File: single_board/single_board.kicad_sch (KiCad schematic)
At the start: 124 parts, among them J1 GPIO, J11 SPI Debug, J17 BOOTSEL, J2 USB_C_Receptacle_USB2.0_16P, J3 SWD, J30 JST_GH_H, J31 JST_GH_H, J33 JST_GH_H, J34 PB_Vertical, J35 JST_GH_H, J36 JST_GH_H, J37 JST_GH_H, J38 PB_Vertical, J39 PB_Vertical, J40 PB_Vertical, J41 PB_Vertical, J42 PB_Vertical, J43 PB_Vertical, J44 PB_Vertical, J45 PB_Vertical, J46 PB_Vertical, J47 PB_Vertical, J48 PB_Vertical, J49 PB_Vertical, J5 JST-GH, J50 PB_Vertical, J53 PB_Vertical, J56 Power, Q1 AO3400A, Q3 AO3401A, SW1 Button, U1 AP2112K-3.3, U3 USBLC6-2SC6, U4 LSM6DSV, U5 STM32G474VBTx, Y2 ABM8-16MHz

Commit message: UART Connector
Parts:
- added J54: (no value), rover:2.54 SMD, symbol Connector_Generic:Conn_01x04
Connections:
- net GND: now also J54.1 (Pin_1), J54.4 (Pin_4)
- net USART3_RX: now also J54.3 (Pin_3)
- net USART3_TX: now also J54.2 (Pin_2)
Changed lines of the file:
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@@
 	)
 	(junction
+		(at 388.62 191.77)
+		(diameter 0)
+		(color 0 0 0 0)
+	)
+	(junction
 		(at 311.15 195.58)
 		(diameter 0)
@@
 	(wire
 		(pts
+			(xy 388.62 191.77) (xy 391.16 191.77)
+		)
+		(stroke
+			(width 0)
+			(type default)
+		)
+	)
+	(wire
+		(pts
 			(xy 153.67 368.3) (xy 156.21 368.3)
 		)
@@
 	(wire
 		(pts
+			(xy 372.11 191.77) (xy 388.62 191.77)
+		)
+		(stroke
+			(width 0)
+			(type default)
+		)
+	)
+	(wire
+		(pts
 			(xy 266.7 91.44) (xy 266.7 92.71)
 		)
@@
 	(wire
 		(pts
-			(xy 384.81 196.85) (xy 391.16 196.85)
-		)
-		(stroke
-			(width 0)
-			(type default)
-		)
-	)
-	(wire
-		(pts
 			(xy 64.77 340.36) (xy 67.31 340.36)
 		)
@@
 	(wire
 		(pts
-			(xy 384.81 194.31) (xy 391.16 194.31)
-		)
-		(stroke
-			(width 0)
-			(type default)
-		)
-	)
-	(wire
-		(pts
 			(xy 388.62 298.45) (xy 392.43 298.45)
 		)
@@
 	(wire
 		(pts
-			(xy 388.62 191.77) (xy 391.16 191.77)
-		)
-		(stroke
-			(width 0)
-			(type default)
-		)
-	)
-	(wire
-		(pts
 			(xy 224.79 287.02) (xy 222.25 287.02)
 		)
@@
 	(wire
 		(pts
+			(xy 372.11 196.85) (xy 391.16 196.85)
+		)
+		(stroke
+			(width 0)
+			(type default)
+		)
+	)
+	(wire
+		(pts
 			(xy 67.31 34.29) (xy 76.2 34.29)
 		)
@@
 	(wire
 		(pts
+			(xy 372.11 194.31) (xy 391.16 194.31)
+		)
+		(stroke
+			(width 0)
+			(type default)
+		)
+	)
+	(wire
+		(pts
 			(xy 274.32 176.53) (xy 278.13 176.53)
 		)
@@
 	(wire
 		(pts
+			(xy 372.11 199.39) (xy 388.62 199.39)
+		)
+		(stroke
+			(width 0)
+			(type default)
+		)
+	)
+	(wire
+		(pts
 			(xy 287.02 190.5) (xy 287.02 193.04)
 		)
@@
 					(unit 1)
 				)
+			)
+		)
+	)
+	(symbol
+		(lib_id "Connector_Generic:Conn_01x04")
+		(at 367.03 194.31 0)
+		(mirror y)
+		(unit 1)
+		(body_style 1)
+		(exclude_from_sim no)
+		(in_bom yes)
+		(on_board yes)
+		(in_pos_files yes)
+		(dnp no)
+		(property "Reference" "J54"
+			(at 364.49 194.3099 0)
+			(show_name no)
+			(do_not_autoplace no)
+			(effects
+				(font
+					(size 1.27 1.27)
+				)
+				(justify left)
+			)
+		)
+		(property "Value" ""
+			(at 364.49 196.8499 0)
+			(show_name no)
+			(do_not_autoplace no)
+			(effects
+				(font
+					(size 1.27 1.27)
+				)
+				(justify left)
+			)
+		)
+		(property "Footprint" "rover:2.54 SMD"
+			(at 367.03 194.31 0)
+			(hide yes)
+			(show_name no)
+			(do_not_autoplace no)
+			(effects
+				(font
+					(size 1.27 1.27)
+				)
+			)
+		)
+		(property "Datasheet" ""
+			(at 367.03 194.31 0)
+			(hide yes)
+			(show_name no)
+			(do_not_autoplace no)
+			(effects
+				(font
+					(size 1.27 1.27)
+				)
+			)
+		)
+		(property "Description" "Generic connector, single row, 01x04, script generated (kicad-library-utils/schlib/autogen/connector/)"
+			(at 367.03 194.31 0)
+			(hide yes)
+			(show_name no)
+			(do_not_autoplace no)
+			(effects
+				(font
+					(size 1.27 1.27)
+				)
+			)
+		)
+		(pin "1"
+		)
+		(pin "3"
+		)
+		(pin "4"
+		)
+		(pin "2"
+		)
+		(instances
+			(project "single_board"
+				(path "/ae10586e-ebf8-402d-a979-c2f011cdeee2"
+					(reference "J54")
+					(unit 1)
+				)

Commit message: GPIO
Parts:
- removed J1: GPIO, Connector_PinHeader_2.54mm:PinHeader_2x04_P2.54mm_Vertical, symbol Connector_Generic:Conn_02x04_Counter_Clockwise
- removed J52: (no value), Connector_PinHeader_2.54mm:PinHeader_1x04_P2.54mm_Vertical, symbol Connector_Generic:Conn_01x04
- added J55, J57: PB_Vertical, Connector_Molex:Molex_PicoBlade_53047-0410_1x04_P1.25mm_Vertical, symbol Connector_Generic:Conn_01x04
- added J6: JST-GH, Connector_JST:JST_GH_SM06B-GHS-TB_1x06-1MP_P1.25mm_Horizontal, symbol Connector_Generic_MountingPin:Conn_01x06_MountingPin
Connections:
- net CAN_LED: now also R1.1; no longer D13.2 (A)
- net GND: now also D13.1 (K), D14.1 (K), J55.1 (Pin_1), J55.4 (Pin_4), J57.1 (Pin_1), J57.4 (Pin_4), J6.1 (Pin_1), J6.6 (Pin_6), J6.MP (MountPin); no longer R1.2, R2.2
- net UART_LED: now also R2.1; no longer D14.2 (A)
- net USART3_RX: now also J55.3 (Pin_3)
- net USART3_TX: now also J55.2 (Pin_2)
- net GPIO_1 renamed I2C4_SCL
- net I2C4_SCL: now also R9.2, J57.3 (Pin_3); no longer R7.2
- net GPIO_2 renamed I2C4_SDA
- net I2C4_SDA: now also R7.2, J57.2 (Pin_2); no longer R9.2
- net GPIO_3: no longer names the net of U5.57 (PD10)
- net GPIO_4: no longer names the net of U5.56 (PD9)
- net GPIO_5 renamed SPI2_NSS
- net SPI2_NSS: now also J6.5 (Pin_5)
- net GPIO_6 renamed SPI2_MOSI
- net SPI2_MOSI: now also J6.4 (Pin_4)
- net GPIO_7 renamed SPI2_MISO
- net SPI2_MISO: now also J6.3 (Pin_3)
- net GPIO_8 renamed SPI2_SCK
- net SPI2_SCK: now also J6.2 (Pin_2)
- net I2C_SCL renamed I2C3_SCL
- net I2C_SDA renamed I2C3_SDA
- new net: D13.2 (A), R1.2
- new net: D14.2 (A), R2.2
- no-connect marks 36 -> 38
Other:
- note added: "Current Sensor"
- note added: "GPIO"
- note removed: "I2C3"
- moved on the sheet: C35, C36, D13, D14, J5, J50, J53, J54, R1, R2, R5, R7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

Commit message: Arm Motor Silkscreen
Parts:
- R7, R9: now fitted
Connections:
- net I2C3_SCL: now also J50.2 (Pin_2), R5.2, U5.67 (PC8); no longer J50.3 (Pin_3), R8.2, U5.69 (PA8)
- net I2C3_SDA: now also J50.3 (Pin_3), R8.2; no longer J50.2 (Pin_2), R5.2
- net I2C4_SCL: now also J57.2 (Pin_2), R7.2; no longer J57.3 (Pin_3), R9.2
- net I2C4_SDA: now also J57.3 (Pin_3), R9.2; no longer J57.2 (Pin_2), R7.2
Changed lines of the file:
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@@
 	)
 	(no_connect
-		(at 302.26 309.88)
-	)
-	(no_connect
 		(at 240.03 44.45)
 	)
@@
 	)
 	(no_connect
+		(at 302.26 223.52)
+	)
+	(no_connect
 		(at 570.23 353.06)
 	)
@@
 	)
 	(label "I2C3_SCL"
-		(at 367.03 260.35 180)
+		(at 367.03 257.81 180)
 		(effects
 			(font
@@
 	)
 	(label "I2C3_SCL"
-		(at 302.26 223.52 0)
+		(at 302.26 309.88 0)
 		(effects
 			(font
@@
 	)
 	(label "I2C4_SDA"
-		(at 372.11 342.9 180)
+		(at 372.11 345.44 180)
 		(effects
 			(font
@@
 	)
 	(label "I2C3_SDA"
-		(at 367.03 257.81 180)
+		(at 367.03 260.35 180)
 		(effects
 			(font
@@
 	)
 	(label "I2C4_SCL"
-		(at 372.11 345.44 180)
+		(at 372.11 342.9 180)
 		(effects
 			(font
@@
 		(on_board yes)
 		(in_pos_files yes)
-		(dnp yes)
+		(dnp no)
 		(property "Reference" "R7"
 			(at 381.508 337.566 0)
@@
 		(on_board yes)
 		(in_pos_files yes)
-		(dnp yes)
+		(dnp no)
 		(property "Reference" "R9"
 			(at 387.858 337.566 0)

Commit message: Routing I2C
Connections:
- net IMU_MOSI: now also J11.3 (Pin_3); no longer J11.4 (Pin_4)
- net IMU_SCK: now also J11.4 (Pin_4); no longer J11.3 (Pin_3)
- net INT1: now also U5.32 (PB0); no longer U5.31 (PC5)
- net INT2: now also U5.31 (PC5); no longer U5.32 (PB0)
- net LED4: now also U5.47 (PB10); no longer U5.46 (PE15)
- net LED5: now also U5.46 (PE15); no longer U5.47 (PB10)
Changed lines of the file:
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@@
 	)
 	(label "LED5"
-		(at 302.26 271.78 0)
-		(effects
-			(font
-				(size 1.27 1.27)
-			)
-			(justify left bottom)
+		(at 256.54 266.7 180)
+		(effects
+			(font
+				(size 1.27 1.27)
+			)
+			(justify right bottom)
 		)
 	)
@@
 	)
 	(label "LED4"
-		(at 256.54 266.7 180)
-		(effects
-			(font
-				(size 1.27 1.27)
-			)
-			(justify right bottom)
+		(at 302.26 271.78 0)
+		(effects
+			(font
+				(size 1.27 1.27)
+			)
+			(justify left bottom)
 		)
 	)
 	(label "IMU_MOSI"
-		(at 506.73 274.32 0)
+		(at 506.73 276.86 0)
 		(effects
 			(font
@@
 	)
 	(label "INT2"
-		(at 302.26 246.38 0)
+		(at 302.26 302.26 0)
 		(effects
 			(font
@@
 	)
 	(label "IMU_SCK"
-		(at 506.73 276.86 0)
+		(at 506.73 274.32 0)
 		(effects
 			(font
@@
 	)
 	(label "INT1"
-		(at 302.26 302.26 0)
-		(effects
-			(font
+		(at 302.26 246.38 0)
+		(effects
+			(font

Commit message: Reanotate
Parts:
- renumbered C30 to C1, C38 to C10, C40 to C11, C39 to C12, C11 to C13, C41 to C14, C14 to C15, C15 to C16, C16 to C17, C17 to C18, C18 to C19, C32 to C2, C19 to C20, C20 to C21, C21 to C22, C22 to C23, C23 to C24, C24 to C25, C25 to C26, C26 to C27, C27 to C28, C12 to C29, C33 to C3, C13 to C30, C28 to C31, C34 to C32, C36 to C33, C35 to C34, C10 to C4, C31 to C5, C3 to C6, C6 to C7, C29 to C8, C37 to C9, D2 to D1, D15 to D10, D13 to D11, D14 to D12, D4 to D2, D1 to D3, D5 to D4, D8 to D5, D9 to D6, D10 to D7, D11 to D8, D12 to D9, J34 to J1, J46 to J10, J41 to J11, J54 to J12, J55 to J13, J47 to J14, J42 to J15, J53 to J16, J5 to J17, J43 to J18, J48 to J19, J3 to J2, J50 to J20, J44 to J21, J49 to J22, J11 to J23, J17 to J24, J6 to J25, J31 to J26, J30 to J27, J36 to J28, J57 to J29, J56 to J3, J37 to J30, J33 to J31, J2 to J4, J35 to J5, J39 to J6, J38 to J7, J40 to J8, J45 to J9, Q3 to Q1, Q1 to Q2, R14 to R1, R11 to R10, R12 to R11, R13 to R12, R16 to R13, R17 to R14, R20 to R15, R1 to R16, R2 to R17, R10 to R18, R15 to R2, R5 to R20, R8 to R21, R26 to R22, R27 to R23, R38 to R24, R21 to R25, R29 to R26, R7 to R27, R9 to R28, R39 to R29, R37 to R3, R22 to R30, R40 to R31, R24 to R32, R41 to R33, R30 to R34, R6 to R5, R23 to R6, R33 to R7, R34 to R8, R31 to R9, U3 to U2, U6 to U3, Y2 to Y1

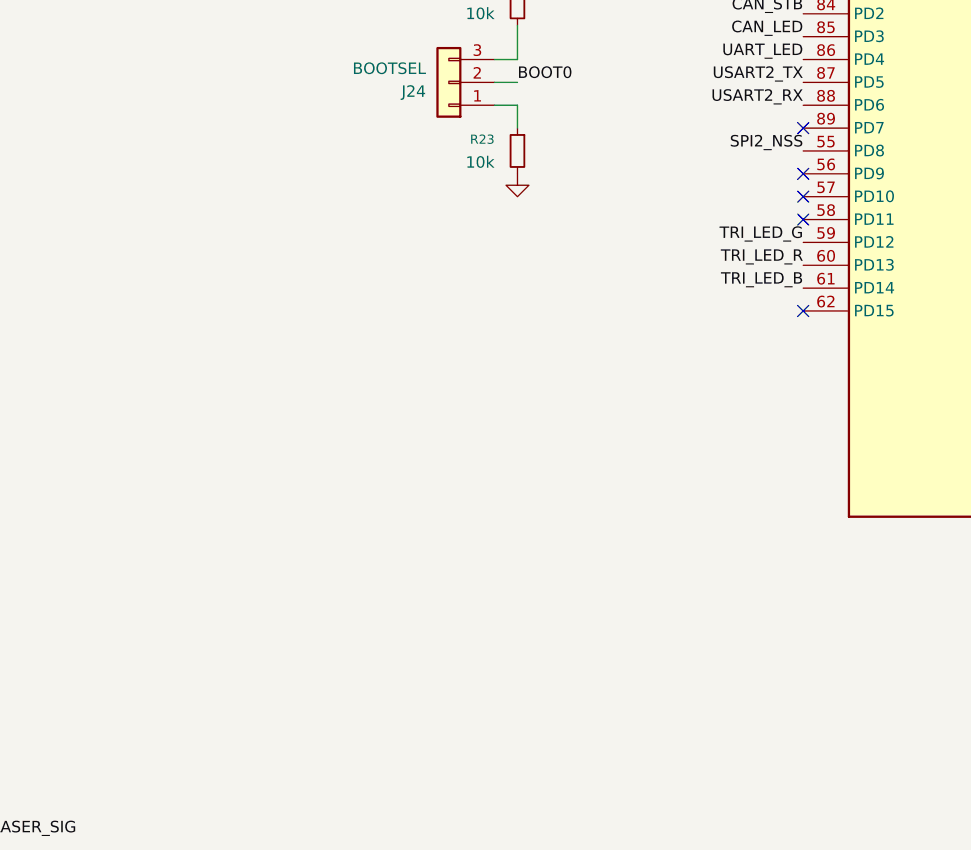
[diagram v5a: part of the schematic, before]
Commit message: 2 User buttons
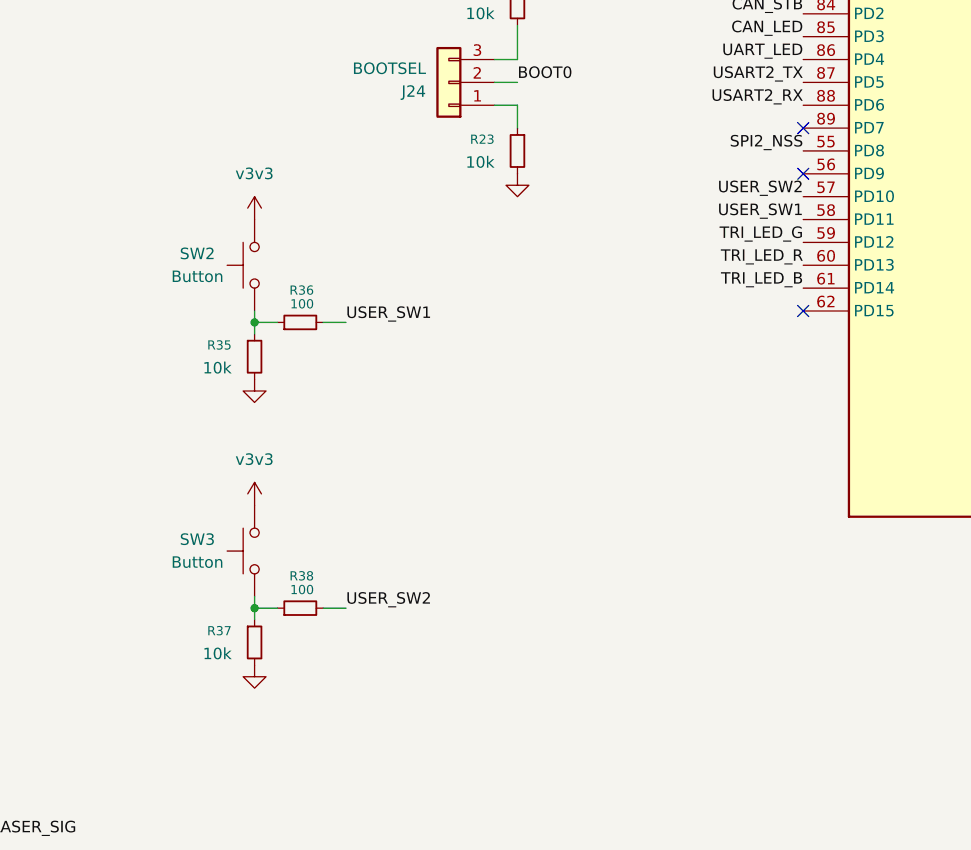
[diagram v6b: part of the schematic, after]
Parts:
- added R35, R37: 10k, Resistor_SMD:R_0402_1005Metric, symbol Device:R_Small
- added R36, R38: 100, Resistor_SMD:R_0402_1005Metric, symbol Device:R_Small
- added SW2, SW3: Button, Button_Switch_SMD:SW_SPST_PTS810, symbol Switch:SW_Push
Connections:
- net GND: now also R35.2, R37.2
- net v3v3: now also SW2.2, SW3.2
- net USER_SW2: now reaches U5.57 (PD10)
- net USER_SW2: now also R38.2
- net USER_SW1: now reaches U5.58 (PD11)
- net USER_SW1: now also R36.2
- new net: R37.1, R38.1, SW3.1
- new net: R35.1, R36.1, SW2.1
- no-connect marks 38 -> 36

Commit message: Production File Setup
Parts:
- C1, C2, C3, C4, C5, C8: LCSC Part # (none) -> C602037
- C10, C11, C13, C20, C21, C22, C23, C24, C28, C29, C30, C31: LCSC Part # (none) -> C100072
- C12, C15, C16, C17, C18, C19, C26, C27, C6, C7, C9: LCSC Part # (none) -> C52923
- C14, C25, C32: LCSC Part # (none) -> C15195
- C33, C34: LCSC Part # (none) -> C76946
- D1, D10, D11, D12, D2, D5, D6, D7, D8, D9: LCSC Part # (none) -> C5160697
- D3: LCSC Part # (none) -> C236208
- D4: LCSC Part # (none) -> C601684
- J1, J10, J11, J13, J14, J15, J16, J18, J19, J20, J21, J22, J29, J6, J7, J8, J9: LCSC Part # (none) -> C504989
- J12: value (none) -> 2.54; now left out of the parts list
- J17, J25: LCSC Part # (none) -> C133065
- J2, J24, TP1, TP2: now left out of the parts list
- J26, J27, J28, J30, J31, J5: value JST_GH_H -> JST_GH; LCSC Part # (none) -> C189893; now left out of the parts list
- J4: LCSC Part # (none) -> C165948
- Q1: LCSC Part # (none) -> C347476
- Q2: LCSC Part # (none) -> C347475
- R1, R10, R11, R12, R13, R14, R15, R16, R17, R18, R19, R2, R22, R23, R25, R30, R32, R34, R35, R37, R6, R9: LCSC Part # (none) -> C71617
- R20, R21, R27, R28, R4, R5: LCSC Part # (none) -> C105872
- R24, R29, R3, R31, R33, R36, R38: LCSC Part # (none) -> C413063
- R26: LCSC Part # (none) -> C26083
- R7, R8: LCSC Part # (none) -> C416565
- SW1, SW2, SW3: LCSC Part # (none) -> C221897
- U1: LCSC Part # (none) -> C51118
- U2: LCSC Part # (none) -> C7519
- U3: value (none) -> TJA1042; LCSC Part # (none) -> C53670; now left out of the parts list
- U4: value LSM6DSV -> LSM6DSVTR; LCSC Part # (none) -> C5267399
- U5: value STM32G474VBTx -> STM32G474VBT6; LCSC Part # (none) -> C730130; now left out of the parts list
- Y1: LCSC Part # (none) -> C179641

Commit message: Remove components
Remove zener diode, pmos
Optimize CAN and power connector
Vias under MCU for better grounding
Fix back silkscreen
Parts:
- removed D3: 3.6V, rover:zener-3v6-onsemi-MMBZ5227BLT1G, symbol Device:D_Zener_Small
- removed Q1: AO3401A, Package_TO_SOT_SMD:SOT-23, symbol Transistor_FET:AO3401A
- removed R3: 100, Resistor_SMD:R_0402_1005Metric, symbol Device:R_Small
- removed R6: 10k, Resistor_SMD:R_0402_1005Metric, symbol Device:R_Small
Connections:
- net v3v3IN is gone; now on net v3v3: J2.1 (Pin_1)
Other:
- note removed: "Reverse input protection"
